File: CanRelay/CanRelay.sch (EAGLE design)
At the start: 13 parts

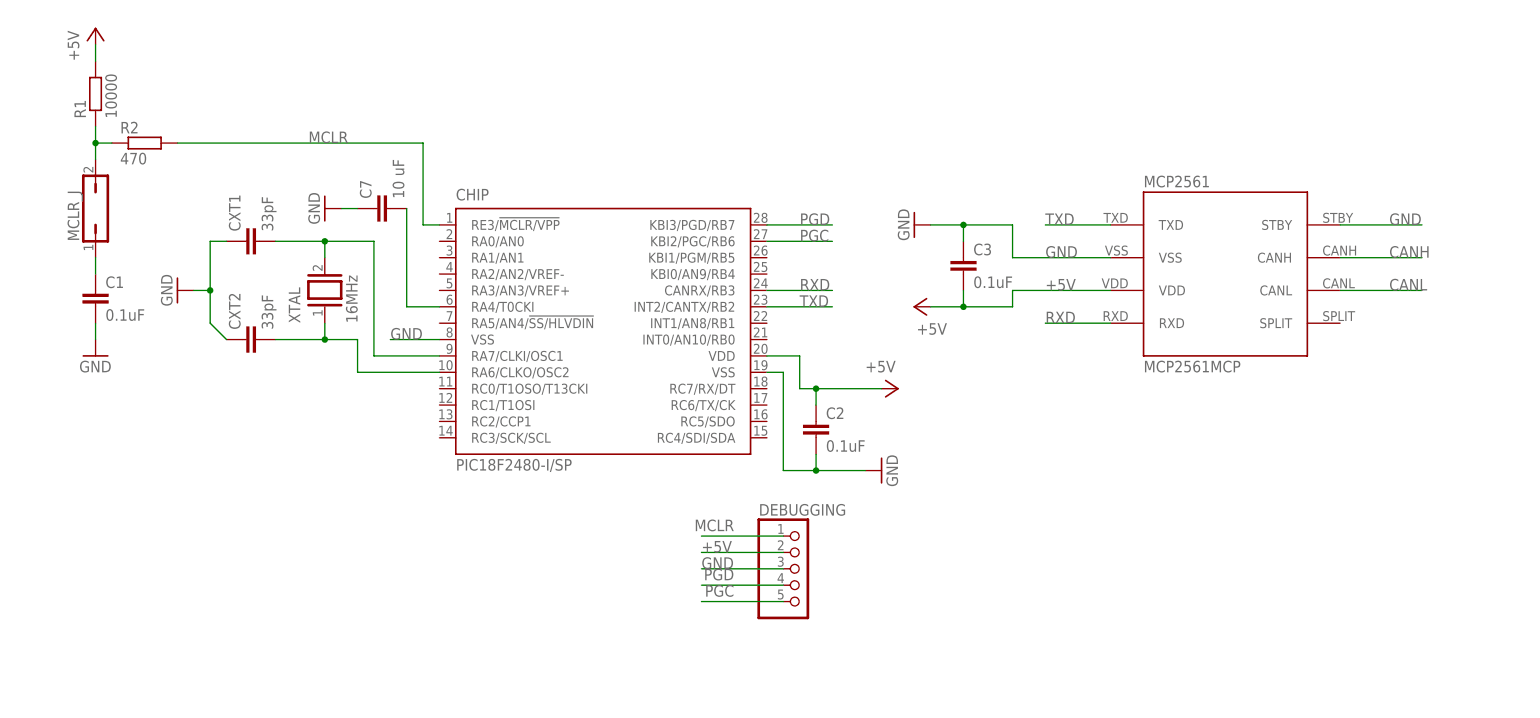
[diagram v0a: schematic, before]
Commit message: #4 adding split pin and resistor termination to can bus as per datasheet. Plus adding all wires to the chip and naming them properly
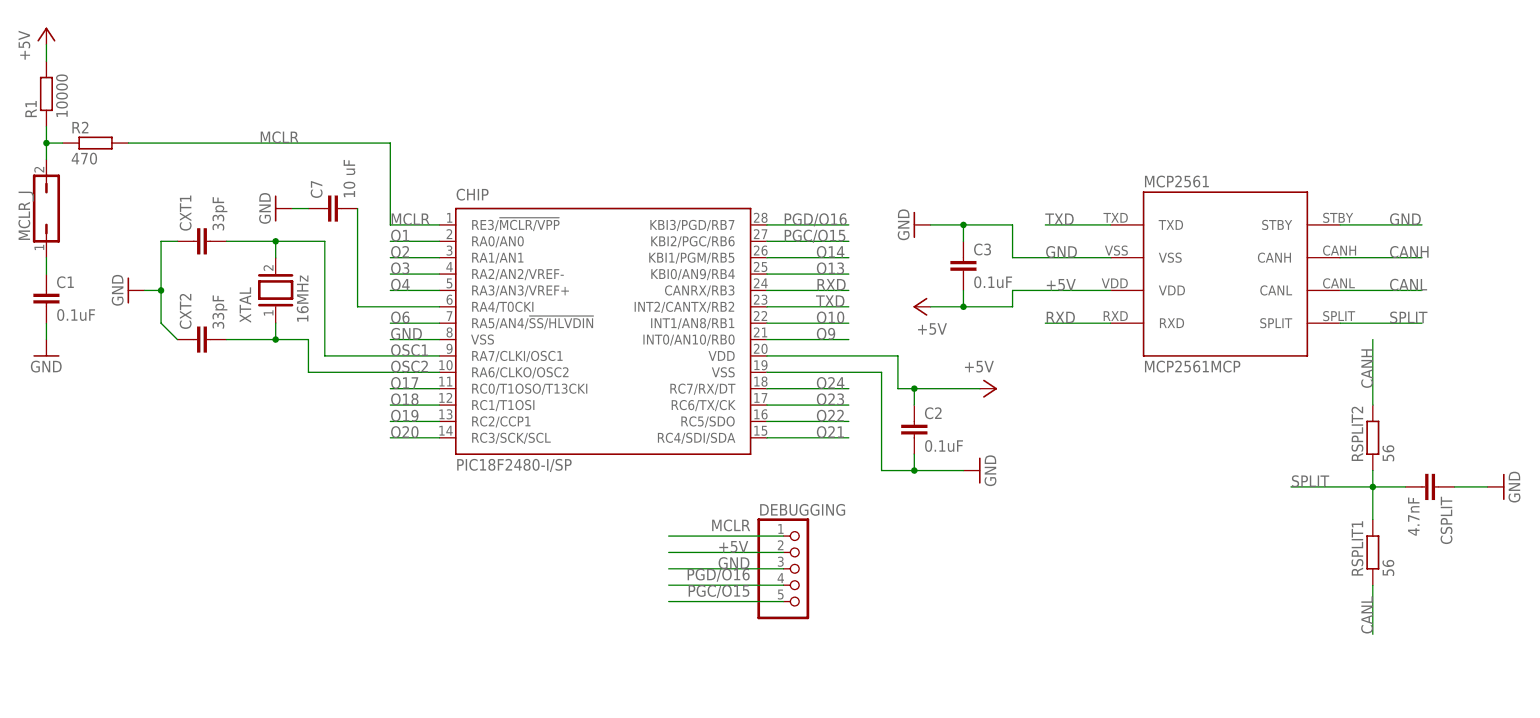
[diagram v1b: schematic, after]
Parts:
- added CSPLIT: 4.7nF, rcl:C-EU025-025X050
- added RSPLIT1, RSPLIT2: 56, rcl:R-EU_0207/10
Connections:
- net N$3 renamed OSC2
- net N$6 renamed OSC1
- net PGC renamed PGC/O15
- net PGD renamed PGD/O16
- new net O1: CHIP.RA0/AN0
- new net O10: CHIP.INT1/AN8/RB1
- new net O13: CHIP.KBI0/AN9/RB4
- new net O14: CHIP.KBI1/PGM/RB5
- new net O17: CHIP.RC0/T1OSO/T13CKI
- new net O18: CHIP.RC1/T1OSI
- new net O19: CHIP.RC2/CCP1
- new net O2: CHIP.RA1/AN1
- new net O20: CHIP.RC3/SCK/SCL
- new net O21: CHIP.RC4/SDI/SDA
- new net O22: CHIP.RC5/SDO
- new net O23: CHIP.RC6/TX/CK
- new net O24: CHIP.RC7/RX/DT
- new net O3: CHIP.RA2/AN2/VREF-
- new net O4: CHIP.RA3/AN3/VREF+
- new net O6: CHIP.RA5/AN4/!SS/HLVDIN
- new net O9: CHIP.INT0/AN10/RB0
- new net SPLIT: CSPLIT.2, MCP2561.SPLIT, RSPLIT1.2, RSPLIT2.1
- net CANH: now also RSPLIT2.2
- net CANL: now also RSPLIT1.1
- net GND: now also CSPLIT.1
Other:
- moved on the sheet: C1, C2, C7, CXT1, CXT2, MCLR_J, R1, R2, XTAL

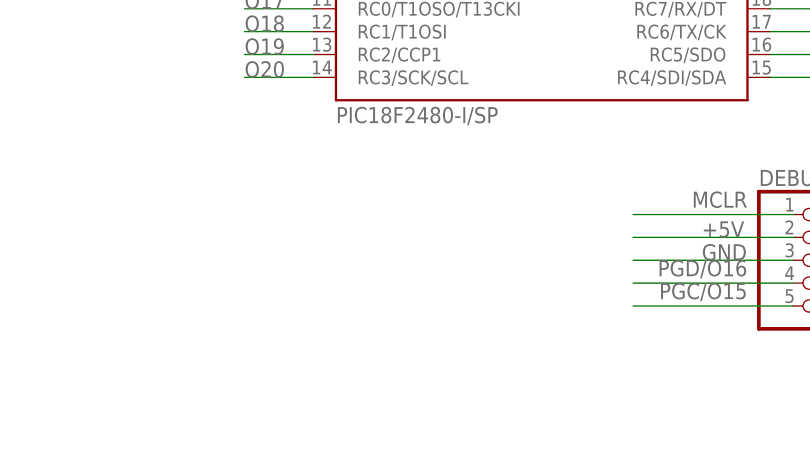
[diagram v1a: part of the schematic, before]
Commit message: #5 added outputs 20pin header from built in library. Added all the wiring to it too, missing new components that need to be added
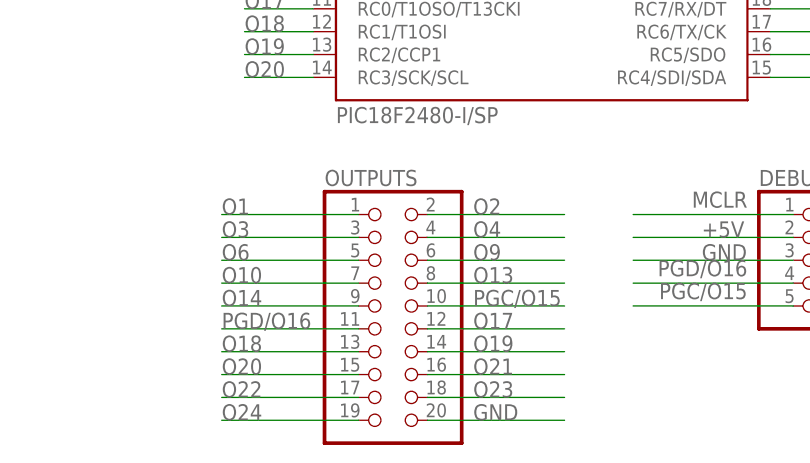
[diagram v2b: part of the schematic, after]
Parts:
- added OUTPUTS: (no value), pinhead:PINHD-2X10
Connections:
- net GND: now also OUTPUTS.20
- net O1: now also OUTPUTS.1
- net O10: now also OUTPUTS.7
- net O13: now also OUTPUTS.8
- net O14: now also OUTPUTS.9
- net O17: now also OUTPUTS.12
- net O18: now also OUTPUTS.13
- net O19: now also OUTPUTS.14
- net O2: now also OUTPUTS.2
- net O20: now also OUTPUTS.15
- net O21: now also OUTPUTS.16
- net O22: now also OUTPUTS.17
- net O23: now also OUTPUTS.18
- net O24: now also OUTPUTS.19
- net O3: now also OUTPUTS.3
- net O4: now also OUTPUTS.4
- net O6: now also OUTPUTS.5
- net O9: now also OUTPUTS.6
- net PGC/O15: now also OUTPUTS.10
- net PGD/O16: now also OUTPUTS.11

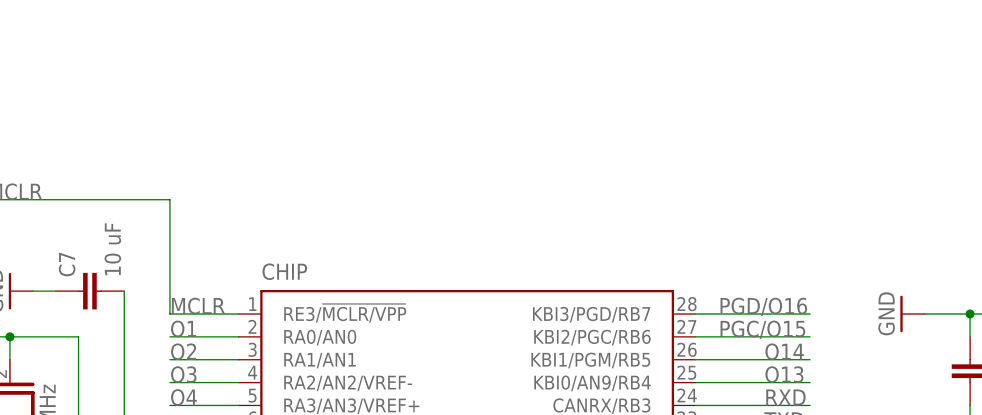
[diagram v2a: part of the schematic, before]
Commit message: #5 new component for RJ45 WEBPP single, also renamed old one to DOUBLE and updated CanSwitch project references, used in CanRelay now and added all the wiring to it too
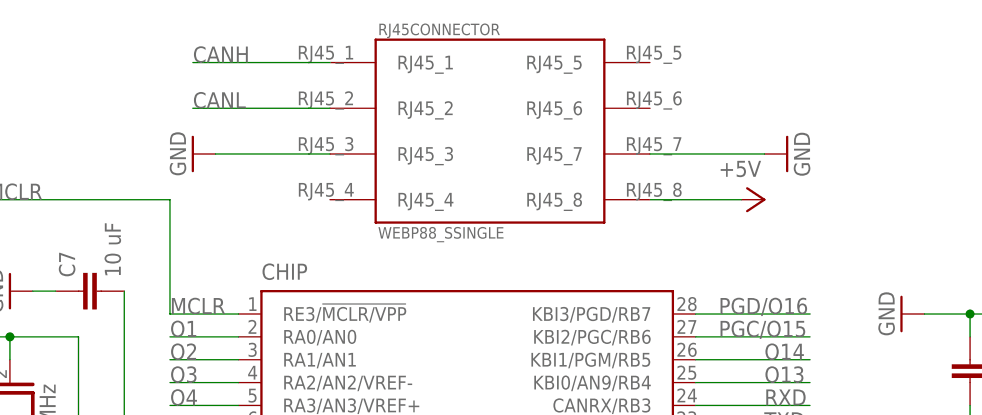
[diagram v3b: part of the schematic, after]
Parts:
- added RJ45CONNECTOR: WEBP88_SSINGLE, PoJD:WEBP88_SSINGLE
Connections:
- net +5V: now also RJ45CONNECTOR.RJ45_8
- net CANH: now also RJ45CONNECTOR.RJ45_1
- net CANL: now also RJ45CONNECTOR.RJ45_2
- net GND: now also RJ45CONNECTOR.RJ45_3, RJ45CONNECTOR.RJ45_7
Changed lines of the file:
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@@
 <grid distance="0.1" unitdist="inch" unit="inch" style="lines" multiple="1" display="no" altdistance="0.01" altunitdist="inch" altunit="inch"/>
 <layers>
-<layer number="1" name="Top" color="4" fill="1" visible="yes" active="no"/>
-<layer number="16" name="Bottom" color="1" fill="1" visible="yes" active="no"/>
-<layer number="17" name="Pads" color="2" fill="1" visible="yes" active="no"/>
-<layer number="18" name="Vias" color="2" fill="1" visible="yes" active="no"/>
-<layer number="19" name="Unrouted" color="6" fill="1" visible="yes" active="no"/>
-<layer number="20" name="Dimension" color="15" fill="1" visible="yes" active="no"/>
-<layer number="21" name="tPlace" color="7" fill="1" visible="yes" active="no"/>
-<layer number="22" name="bPlace" color="7" fill="1" visible="yes" active="no"/>
-<layer number="23" name="tOrigins" color="15" fill="1" visible="yes" active="no"/>
-<layer number="24" name="bOrigins" color="15" fill="1" visible="yes" active="no"/>
-<layer number="25" name="tNames" color="7" fill="1" visible="yes" active="no"/>
-<layer number="26" name="bNames" color="7" fill="1" visible="yes" active="no"/>
-<layer number="27" name="tValues" color="7" fill="1" visible="yes" active="no"/>
-<layer number="28" name="bValues" color="7" fill="1" visible="yes" active="no"/>
+<layer number="1" name="Top" color="4" fill="1" visible="no" active="no"/>
+<layer number="16" name="Bottom" color="1" fill="1" visible="no" active="no"/>
+<layer number="17" name="Pads" color="2" fill="1" visible="no" active="no"/>
+<layer number="18" name="Vias" color="2" fill="1" visible="no" active="no"/>
+<layer number="19" name="Unrouted" color="6" fill="1" visible="no" active="no"/>
+<layer number="20" name="Dimension" color="15" fill="1" visible="no" active="no"/>
+<layer number="21" name="tPlace" color="7" fill="1" visible="no" active="no"/>
+<layer number="22" name="bPlace" color="7" fill="1" visible="no" active="no"/>
+<layer number="23" name="tOrigins" color="15" fill="1" visible="no" active="no"/>
+<layer number="24" name="bOrigins" color="15" fill="1" visible="no" active="no"/>
+<layer number="25" name="tNames" color="7" fill="1" visible="no" active="no"/>
+<layer number="26" name="bNames" color="7" fill="1" visible="no" active="no"/>
+<layer number="27" name="tValues" color="7" fill="1" visible="no" active="no"/>
+<layer number="28" name="bValues" color="7" fill="1" visible="no" active="no"/>
 <layer number="29" name="tStop" color="7" fill="3" visible="no" active="no"/>
 <layer number="30" name="bStop" color="7" fill="6" visible="no" active="no"/>
@@
 <layer number="35" name="tGlue" color="7" fill="4" visible="no" active="no"/>
 <layer number="36" name="bGlue" color="7" fill="5" visible="no" active="no"/>
-<layer number="37" name="tTest" color="7" fill="1" visible="yes" active="no"/>
-<layer number="38" name="bTest" color="7" fill="1" visible="yes" active="no"/>
+<layer number="37" name="tTest" color="7" fill="1" visible="no" active="no"/>
+<layer number="38" name="bTest" color="7" fill="1" visible="no" active="no"/>
 <layer number="39" name="tKeepout" color="4" fill="11" visible="no" active="no"/>
 <layer number="40" name="bKeepout" color="1" fill="11" visible="no" active="no"/>
@@
 <layer number="44" name="Drills" color="7" fill="1" visible="no" active="no"/>
 <layer number="45" name="Holes" color="7" fill="1" visible="no" active="no"/>
-<layer number="46" name="Milling" color="3" fill="1" visible="yes" active="no"/>
-<layer number="47" name="Measures" color="7" fill="1" visible="yes" active="no"/>
-<layer number="48" name="Document" color="7" fill="1" visible="yes" active="no"/>
-<layer number="49" name="Reference" color="7" fill="1" visible="yes" active="no"/>
-<layer number="51" name="tDocu" color="7" fill="1" visible="yes" active="no"/>
-<layer number="52" name="bDocu" color="7" fill="1" visible="yes" active="no"/>
+<layer number="46" name="Milling" color="3" fill="1" visible="no" active="no"/>
+<layer number="47" name="Measures" color="7" fill="1" visible="no" active="no"/>
+<layer number="48" name="Document" color="7" fill="1" visible="no" active="no"/>
+<layer number="49" name="Reference" color="7" fill="1" visible="no" active="no"/>
+<layer number="51" name="tDocu" color="7" fill="1" visible="no" active="no"/>
+<layer number="52" name="bDocu" color="7" fill="1" visible="no" active="no"/>
 <layer number="90" name="Modules" color="5" fill="1" visible="yes" active="yes"/>
 <layer number="91" name="Nets" color="2" fill="1" visible="yes" active="yes"/>
@@
 <part name="GND1" library="supply1" deviceset="GND" device=""/>
 <part name="OUTPUTS" library="pinhead" deviceset="PINHD-2X10" device=""/>
+<part name="RJ45CONNECTOR" library="PoJD" deviceset="WEBP88_S" device="SINGLE"/>
+<part name="P+4" library="supply1" deviceset="+5V" device=""/>
+<part name="GND7" library="supply1" deviceset="GND" device=""/>
+<part name="GND8" library="supply1" deviceset="GND" device=""/>
 </parts>
 <sheets>
@@
 <instance part="GND1" gate="1" x="63.5" y="63.5" rot="R90"/>
 <instance part="OUTPUTS" gate="A" x="-93.98" y="45.72"/>
+<instance part="RJ45CONNECTOR" gate="G$1" x="-73.66" y="124.46"/>
+<instance part="P+4" gate="1" x="-43.18" y="116.84" rot="R270"/>
+<instance part="GND7" gate="1" x="-40.64" y="121.92" rot="R90"/>
+<instance part="GND8" gate="1" x="-106.68" y="121.92" rot="R270"/>
 </instances>
 <busses>
@@
 <label x="-58.42" y="53.34" size="1.778" layer="95"/>
 </segment>
+<segment>
+<pinref part="RJ45CONNECTOR" gate="G$1" pin="RJ45_8"/>
+<pinref part="P+4" gate="1" pin="+5V"/>
+<wire x1="-55.88" y1="116.84" x2="-45.72" y2="116.84" width="0.1524" layer="91"/>
+</segment>
 </net>
 <net name="GND" class="0">
@@
 <label x="-83.82" y="33.02" size="1.778" layer="95"/>
 </segment>
+<segment>
+<pinref part="RJ45CONNECTOR" gate="G$1" pin="RJ45_7"/>
+<pinref part="GND7" gate="1" pin="GND"/>
+<wire x1="-55.88" y1="121.92" x2="-43.18" y2="121.92" width="0.1524" layer="91"/>
+</segment>
+<segment>
+<pinref part="RJ45CONNECTOR" gate="G$1" pin="RJ45_3"/>
+<pinref part="GND8" gate="1" pin="GND"/>
+<wire x1="-91.44" y1="121.92" x2="-104.14" y2="121.92" width="0.1524" layer="91"/>
+</segment>
 </net>
 <net name="N$2" class="0">
@@
 <label x="43.18" y="78.74" size="1.778" layer="95" rot="R90"/>
 </segment>
+<segment>
+<pinref part="RJ45CONNECTOR" gate="G$1" pin="RJ45_1"/>
+<wire x1="-91.44" y1="132.08" x2="-106.68" y2="132.08" width="0.1524" layer="91"/>
+<label x="-106.68" y="132.08" size="1.778" layer="95"/>
+</segment>
 </net>
 <net name="CANL" class="0">
@@
 <label x="43.18" y="40.64" size="1.778" layer="95" rot="R90"/>
 </segment>
-</net>
+<segment>
+<pinref part="RJ45CONNECTOR" gate="G$1" pin="RJ45_2"/>
+<wire x1="-91.44" y1="127" x2="-106.68" y2="127" width="0.1524" layer="91"/>
+<label x="-106.68" y="127" size="1.778" layer="95"/>
+</segment>
+</net>

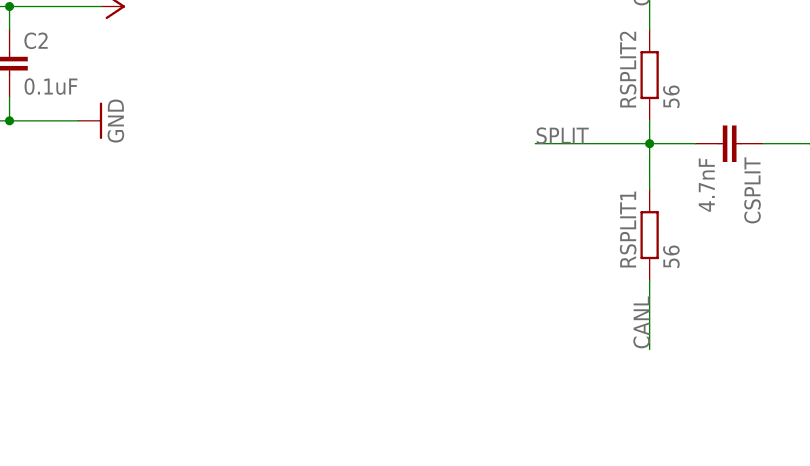
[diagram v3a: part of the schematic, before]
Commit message: #5 adding USBTIN 3pin connector (new component in the library)
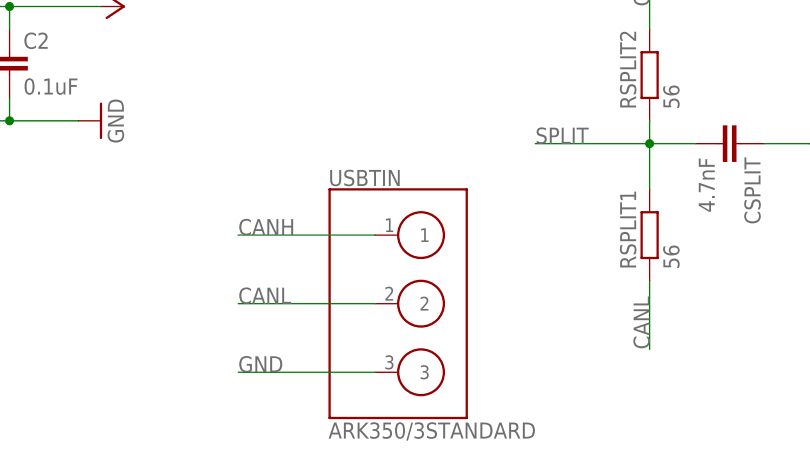
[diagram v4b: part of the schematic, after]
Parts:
- added USBTIN: ARK350/3STANDARD, PoJD:ARK350/3STANDARD
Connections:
- net CANH: now also USBTIN.1
- net CANL: now also USBTIN.2
- net GND: now also USBTIN.3
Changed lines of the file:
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@@
 <part name="GND7" library="supply1" deviceset="GND" device=""/>
 <part name="GND8" library="supply1" deviceset="GND" device=""/>
+<part name="USBTIN" library="PoJD" deviceset="ARK350/3" device="STANDARD"/>
 </parts>
 <sheets>
@@
 <instance part="GND7" gate="1" x="-40.64" y="121.92" rot="R90"/>
 <instance part="GND8" gate="1" x="-106.68" y="121.92" rot="R270"/>
+<instance part="USBTIN" gate="G$1" x="15.24" y="45.72"/>
 </instances>
 <busses>
@@
 <wire x1="-91.44" y1="121.92" x2="-104.14" y2="121.92" width="0.1524" layer="91"/>
 </segment>
+<segment>
+<pinref part="USBTIN" gate="G$1" pin="3"/>
+<wire x1="12.7" y1="38.1" x2="-2.54" y2="38.1" width="0.1524" layer="91"/>
+<label x="-2.54" y="38.1" size="1.778" layer="95"/>
+</segment>
 </net>
 <net name="N$2" class="0">
@@
 <label x="-106.68" y="132.08" size="1.778" layer="95"/>
 </segment>
+<segment>
+<pinref part="USBTIN" gate="G$1" pin="1"/>
+<wire x1="12.7" y1="53.34" x2="-2.54" y2="53.34" width="0.1524" layer="91"/>
+<label x="-2.54" y="53.34" size="1.778" layer="95"/>
+</segment>
 </net>
 <net name="CANL" class="0">
@@
 <label x="-106.68" y="127" size="1.778" layer="95"/>
 </segment>
-</net>
+<segment>
+<pinref part="USBTIN" gate="G$1" pin="2"/>
+<wire x1="12.7" y1="45.72" x2="-2.54" y2="45.72" width="0.1524" layer="91"/>
+<label x="-2.54" y="45.72" size="1.778" layer="95"/>
+</segment>
+</net>
